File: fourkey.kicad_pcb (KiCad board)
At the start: 2 copper layers, 85.3 x 75.7 mm, 20 parts, among them K1 KEYSW, K2 KEYSW, K3 KEYSW, K4 KEYSW, SW1 SW_PUSH, U1 ProMicro

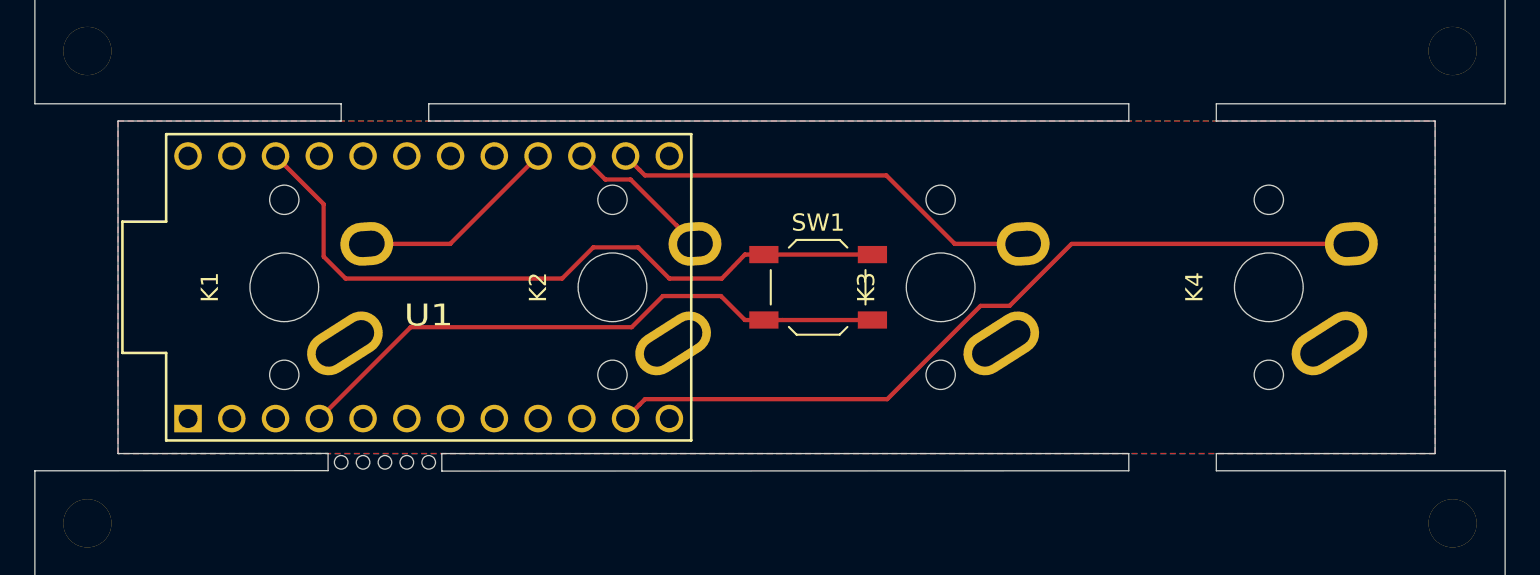
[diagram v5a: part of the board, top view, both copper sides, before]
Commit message: add other mousebites, rounded corners
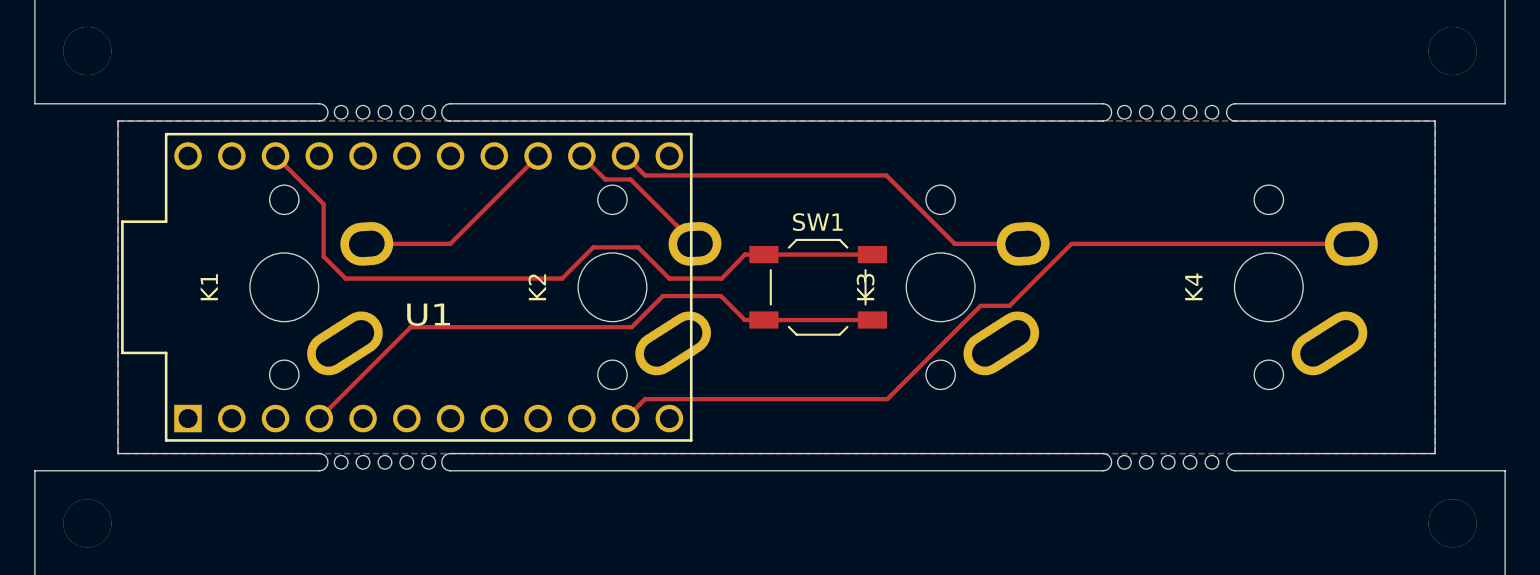
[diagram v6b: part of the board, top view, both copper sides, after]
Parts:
- added REF**: breakaway-mousebites, Keebio-Parts:breakaway-mousebites, F.Cu at (147.3, 76.5)
- added REF**: breakaway-mousebites, Keebio-Parts:breakaway-mousebites, F.Cu at (192.8, 76.5)
- added REF**: breakaway-mousebites, Keebio-Parts:breakaway-mousebites, F.Cu at (192.8, 96.8)
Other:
- outline, holes or cut-outs redrawn
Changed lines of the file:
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@@
   (general
     (thickness 1.6)
-    (drawings 35)
+    (drawings 28)
     (tracks 38)
     (zones 0)
-    (modules 20)
+    (modules 23)
     (nets 27)
   )
@@
     (add_net "Net-(U1-Pad9)")
     (add_net VCC)
+  )
+  (module Keebio-Parts:breakaway-mousebites (layer F.Cu)
+    (at 147.32 76.454)
+    (fp_text reference REF** (at 0 -3.048) (layer Dwgs.User) hide
+      (effects (font (size 1 1) (thickness 0.15)))
+    )
+    (fp_text value breakaway-mousebites (at 0 -4.75) (layer F.Fab) hide
+      (effects (font (size 1 1) (thickness 0.15)))
+    )
+    (fp_line (start -2.794 0) (end 2.794 0) (layer Dwgs.User) (width 0.15))
+    (pad "" np_thru_hole circle (at -2.54 -0.254) (size 0.7874 0.7874) (drill 0.7874) (layers *.Cu *.Mask))
+    (pad "" np_thru_hole circle (at -1.27 -0.254) (size 0.7874 0.7874) (drill 0.7874) (layers *.Cu *.Mask))
+    (pad "" np_thru_hole circle (at 2.54 -0.254) (size 0.7874 0.7874) (drill 0.7874) (layers *.Cu *.Mask))
+    (pad "" np_thru_hole circle (at 1.27 -0.254) (size 0.7874 0.7874) (drill 0.7874) (layers *.Cu *.Mask))
+    (pad "" np_thru_hole circle (at 0 -0.254) (size 0.7874 0.7874) (drill 0.7874) (layers *.Cu *.Mask))
+  )
+  (module Keebio-Parts:breakaway-mousebites (layer F.Cu)
+    (at 192.786 76.454)
+    (fp_text reference REF** (at 0 -3.048) (layer Dwgs.User) hide
+      (effects (font (size 1 1) (thickness 0.15)))
+    )
+    (fp_text value breakaway-mousebites (at 0 -4.75) (layer F.Fab) hide
+      (effects (font (size 1 1) (thickness 0.15)))
+    )
+    (fp_line (start -2.794 0) (end 2.794 0) (layer Dwgs.User) (width 0.15))
+    (pad "" np_thru_hole circle (at -2.54 -0.254) (size 0.7874 0.7874) (drill 0.7874) (layers *.Cu *.Mask))
+    (pad "" np_thru_hole circle (at -1.27 -0.254) (size 0.7874 0.7874) (drill 0.7874) (layers *.Cu *.Mask))
+    (pad "" np_thru_hole circle (at 2.54 -0.254) (size 0.7874 0.7874) (drill 0.7874) (layers *.Cu *.Mask))
+    (pad "" np_thru_hole circle (at 1.27 -0.254) (size 0.7874 0.7874) (drill 0.7874) (layers *.Cu *.Mask))
+    (pad "" np_thru_hole circle (at 0 -0.254) (size 0.7874 0.7874) (drill 0.7874) (layers *.Cu *.Mask))
+  )
+  (module Keebio-Parts:breakaway-mousebites (layer F.Cu)
+    (at 192.786 96.774)
+    (fp_text reference REF** (at 0 -3.048) (layer Dwgs.User) hide
+      (effects (font (size 1 1) (thickness 0.15)))
+    )
+    (fp_text value breakaway-mousebites (at 0 -4.75) (layer F.Fab) hide
+      (effects (font (size 1 1) (thickness 0.15)))
+    )
+    (fp_line (start -2.794 0) (end 2.794 0) (layer Dwgs.User) (width 0.15))
+    (pad "" np_thru_hole circle (at -2.54 -0.254) (size 0.7874 0.7874) (drill 0.7874) (layers *.Cu *.Mask))
+    (pad "" np_thru_hole circle (at -1.27 -0.254) (size 0.7874 0.7874) (drill 0.7874) (layers *.Cu *.Mask))
+    (pad "" np_thru_hole circle (at 2.54 -0.254) (size 0.7874 0.7874) (drill 0.7874) (layers *.Cu *.Mask))
+    (pad "" np_thru_hole circle (at 1.27 -0.254) (size 0.7874 0.7874) (drill 0.7874) (layers *.Cu *.Mask))
+    (pad "" np_thru_hole circle (at 0 -0.254) (size 0.7874 0.7874) (drill 0.7874) (layers *.Cu *.Mask))
   )
   (module keyboard_parts:HOLE_M3 (layer F.Cu)
@@
     )
   )
+  (gr_arc (start 151.122 76.208) (end 151.122 75.708) (angle -180) (layer Edge.Cuts) (width 0.05))
+  (gr_arc (start 143.51 76.208) (end 143.51 75.708) (angle 180) (layer Edge.Cuts) (width 0.05))
+  (gr_arc (start 196.68 76.208) (end 196.68 75.708) (angle -180) (layer Edge.Cuts) (width 0.05))
+  (gr_arc (start 189 76.208) (end 189 75.708) (angle 180) (layer Edge.Cuts) (width 0.05))
+  (gr_arc (start 196.68 96.512) (end 196.68 96.012001) (angle -180) (layer Edge.Cuts) (width 0.05))
+  (gr_arc (start 189 96.512) (end 189 96.012001) (angle 180) (layer Edge.Cuts) (width 0.05))
+  (gr_arc (start 151.122 96.512) (end 151.122 96.012) (angle -180) (layer Edge.Cuts) (width 0.05))
+  (gr_arc (start 143.51 96.512) (end 143.51 96.012) (angle 180) (layer Edge.Cuts) (width 0.05))
   (gr_line (start 212.344 124.19) (end 127 124.19) (layer Edge.Cuts) (width 0.05))
-  (gr_line (start 195.58 96.52) (end 195.58 96.52) (layer Edge.Cuts) (width 0.05))
   (gr_line (start 212.344 97.012) (end 212.344 124.19) (layer Edge.Cuts) (width 0.05))
-  (gr_line (start 190.5 96.012) (end 190.5 97.012) (layer Edge.Cuts) (width 0.05))
-  (gr_line (start 190.5 96.52) (end 190.5 96.52) (layer Edge.Cuts) (width 0.05))
-  (gr_line (start 127 97.012) (end 144.018 97.004) (layer Edge.Cuts) (width 0.05))
+  (gr_line (start 127 97.012) (end 143.51 97.012) (layer Edge.Cuts) (width 0.05))
   (gr_line (start 127 97.012) (end 127 124.19) (layer Edge.Cuts) (width 0.05))
-  (gr_line (start 150.622 96.012) (end 150.622 97.028) (layer Edge.Cuts) (width 0.05))
-  (gr_line (start 195.58 96.012) (end 195.58 97.012) (layer Edge.Cuts) (width 0.05))
-  (gr_line (start 195.58 97.012) (end 212.344 97.012) (layer Edge.Cuts) (width 0.05))
-  (gr_line (start 144.018 96.004) (end 144.018 97.004) (layer Edge.Cuts) (width 0.05))
-  (gr_line (start 150.622 97.028) (end 190.5 97.012) (layer Edge.Cuts) (width 0.05))
-  (gr_line (start 195.58 96.52) (end 195.58 96.52) (layer Edge.Cuts) (width 0.05))
-  (gr_line (start 195.58 96.012) (end 208.28 96.012) (layer Edge.Cuts) (width 0.05))
-  (gr_line (start 150.622 96.012) (end 190.5 96.012) (layer Edge.Cuts) (width 0.05))
-  (gr_line (start 195.58 75.708) (end 195.58 76.708) (layer Edge.Cuts) (width 0.05))
-  (gr_line (start 190.5 75.708) (end 190.5 76.708) (layer Edge.Cuts) (width 0.05))
-  (gr_line (start 190.5 76.708) (end 149.86 76.708) (layer Edge.Cuts) (width 0.05))
-  (gr_line (start 190.5 75.692) (end 190.5 75.692) (layer Edge.Cuts) (width 0.05))
-  (gr_line (start 195.58 75.692) (end 195.58 75.692) (layer Edge.Cuts) (width 0.05))
-  (gr_line (start 195.58 75.708) (end 212.344 75.708) (layer Edge.Cuts) (width 0.05))
-  (gr_line (start 144.78 76.708) (end 131.826 76.708) (layer Edge.Cuts) (width 0.05))
-  (gr_line (start 149.86 75.692) (end 149.86 75.692) (layer Edge.Cuts) (width 0.05))
-  (gr_line (start 149.86 75.708) (end 190.5 75.708) (layer Edge.Cuts) (width 0.05))
-  (gr_line (start 149.86 75.692) (end 149.86 75.692) (layer Edge.Cuts) (width 0.05))
-  (gr_line (start 149.86 75.708) (end 149.86 76.708) (layer Edge.Cuts) (width 0.05))
-  (gr_line (start 144.78 76.708) (end 144.78 75.708) (layer Edge.Cuts) (width 0.05))
+  (gr_line (start 196.68 97.012) (end 212.344 97.012) (layer Edge.Cuts) (width 0.05))
+  (gr_line (start 151.122 97.012) (end 189 97.012) (layer Edge.Cuts) (width 0.05))
+  (gr_line (start 196.68 96.012) (end 208.28 96.012) (layer Edge.Cuts) (width 0.05))
+  (gr_line (start 151.122 96.012) (end 189 96.012) (layer Edge.Cuts) (width 0.05))
+  (gr_line (start 189 76.708) (end 151.122 76.708) (layer Edge.Cuts) (width 0.05))
+  (gr_line (start 196.68 75.708) (end 212.344 75.708) (layer Edge.Cuts) (width 0.05))
+  (gr_line (start 143.51 76.708) (end 131.826 76.708) (layer Edge.Cuts) (width 0.05))
+  (gr_line (start 151.122 75.708) (end 189 75.708) (layer Edge.Cuts) (width 0.05))
   (gr_line (start 212.344 48.53) (end 127 48.53) (layer Edge.Cuts) (width 0.05))
   (gr_line (start 127 48.53) (end 127 75.708) (layer Edge.Cuts) (width 0.05))
-  (gr_line (start 127 75.708) (end 144.78 75.708) (layer Edge.Cuts) (width 0.05))
+  (gr_line (start 127 75.708) (end 143.51 75.708) (layer Edge.Cuts) (width 0.05))
   (gr_line (start 212.344 75.708) (end 212.344 48.53) (layer Edge.Cuts) (width 0.05))
   (gr_line (start 208.28 96.012) (end 208.28 76.708) (layer Edge.Cuts) (width 0.05))
-  (gr_line (start 131.826 96.012) (end 144.018 96.004) (layer Edge.Cuts) (width 0.05))
+  (gr_line (start 131.826 96.012) (end 143.51 96.012) (layer Edge.Cuts) (width 0.05))
   (gr_line (start 131.826 76.708) (end 131.826 96.012) (layer Edge.Cuts) (width 0.05))
-  (gr_line (start 208.28 76.708) (end 195.58 76.708) (layer Edge.Cuts) (width 0.05))
+  (gr_line (start 208.28 76.708) (end 196.68 76.708) (layer Edge.Cuts) (width 0.05))
   (segment (start 151.11 83.84) (end 156.21 78.74) (width 0.25) (layer F.Cu) (net 2))
   (segment (start 146.268 83.84) (end 151.11 83.84) (width 0.25) (layer F.Cu) (net 2))

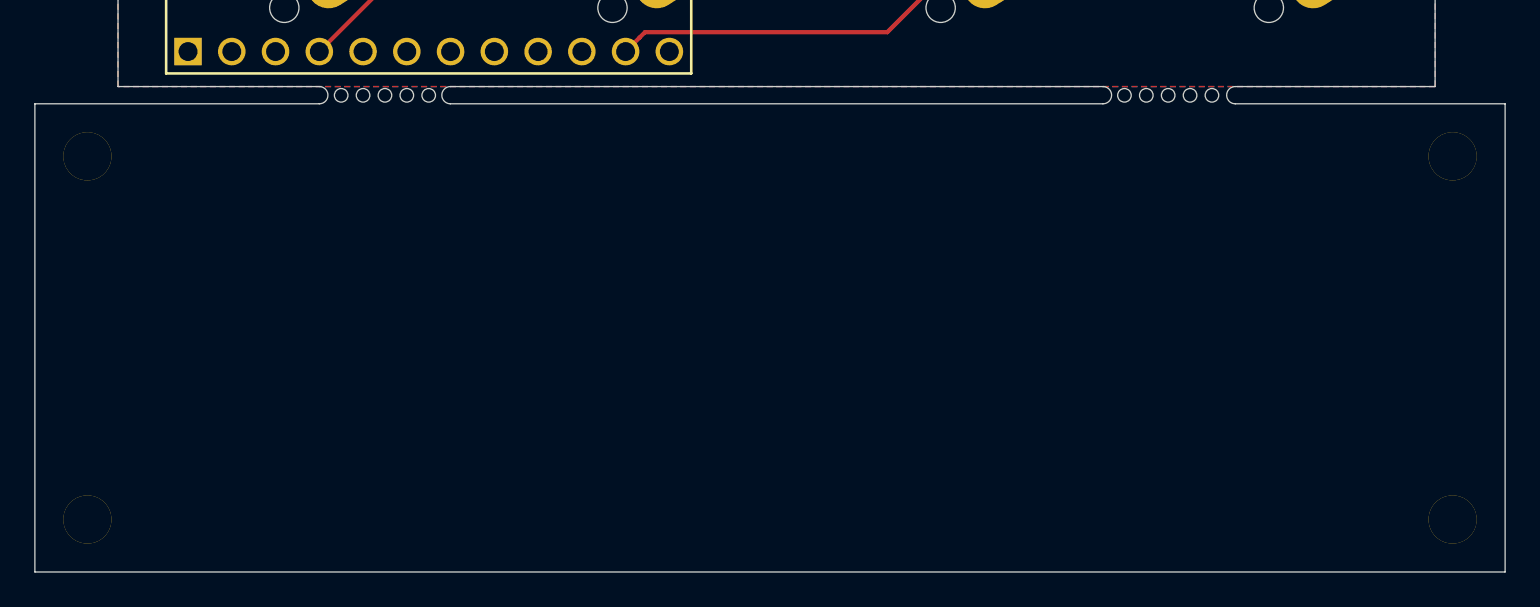
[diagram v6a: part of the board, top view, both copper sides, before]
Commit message: more rounded corners
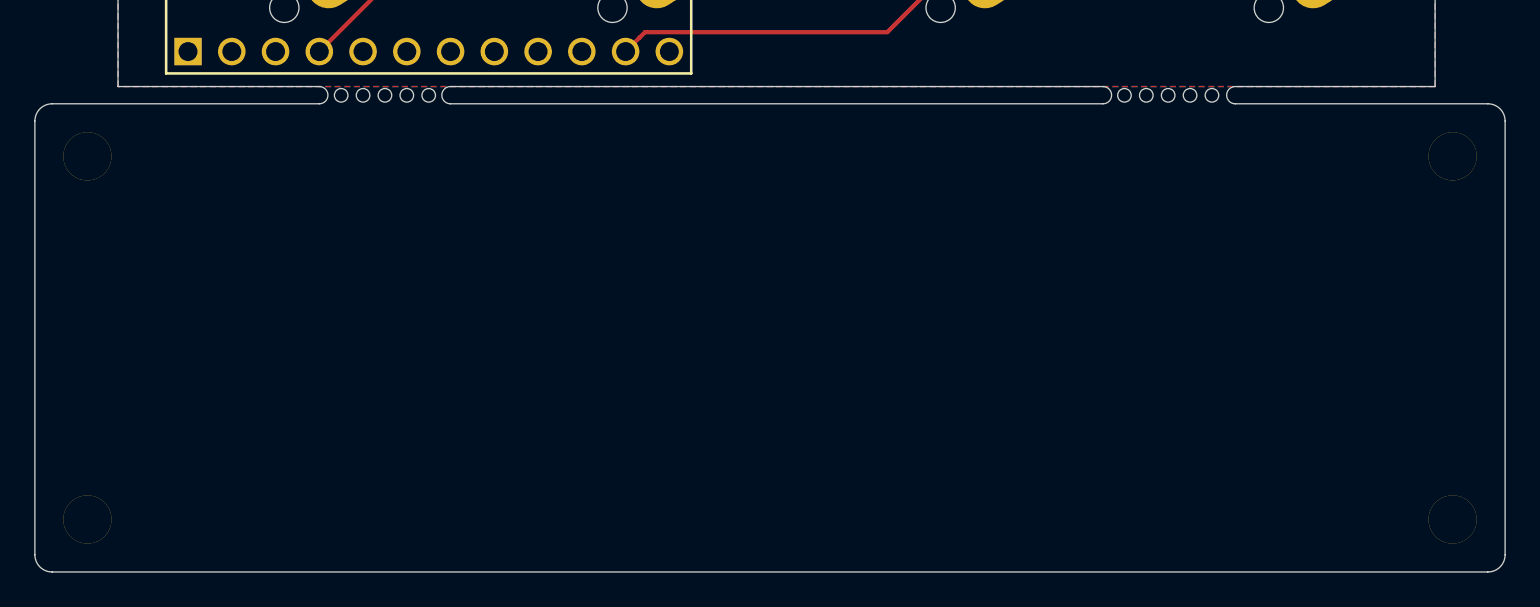
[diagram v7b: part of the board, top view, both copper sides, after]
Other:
- outline, holes or cut-outs redrawn
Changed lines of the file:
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@@
   (general
     (thickness 1.6)
-    (drawings 28)
+    (drawings 32)
     (tracks 38)
     (zones 0)
@@
     )
   )
+  (gr_arc (start 211.344 98.012) (end 212.344 98.012) (angle -90) (layer Edge.Cuts) (width 0.05))
+  (gr_arc (start 211.344 123.19) (end 212.344 123.19) (angle 90) (layer Edge.Cuts) (width 0.05))
+  (gr_arc (start 128 123.19) (end 127 123.19) (angle -90) (layer Edge.Cuts) (width 0.05))
+  (gr_arc (start 128 98.012) (end 128 97.012) (angle -90) (layer Edge.Cuts) (width 0.05))
   (gr_arc (start 151.122 76.208) (end 151.122 75.708) (angle -180) (layer Edge.Cuts) (width 0.05))
   (gr_arc (start 143.51 76.208) (end 143.51 75.708) (angle 180) (layer Edge.Cuts) (width 0.05))
@@
   (gr_arc (start 151.122 96.512) (end 151.122 96.012) (angle -180) (layer Edge.Cuts) (width 0.05))
   (gr_arc (start 143.51 96.512) (end 143.51 96.012) (angle 180) (layer Edge.Cuts) (width 0.05))
-  (gr_line (start 212.344 124.19) (end 127 124.19) (layer Edge.Cuts) (width 0.05))
-  (gr_line (start 212.344 97.012) (end 212.344 124.19) (layer Edge.Cuts) (width 0.05))
-  (gr_line (start 127 97.012) (end 143.51 97.012) (layer Edge.Cuts) (width 0.05))
-  (gr_line (start 127 97.012) (end 127 124.19) (layer Edge.Cuts) (width 0.05))
-  (gr_line (start 196.68 97.012) (end 212.344 97.012) (layer Edge.Cuts) (width 0.05))
+  (gr_line (start 211.344 124.19) (end 128 124.19) (layer Edge.Cuts) (width 0.05))
+  (gr_line (start 212.344 98.012) (end 212.344 123.19) (layer Edge.Cuts) (width 0.05))
+  (gr_line (start 128 97.012) (end 143.51 97.012) (layer Edge.Cuts) (width 0.05))
+  (gr_line (start 127 98.012) (end 127 123.19) (layer Edge.Cuts) (width 0.05))
+  (gr_line (start 196.68 97.012) (end 211.344 97.012) (layer Edge.Cuts) (width 0.05))
   (gr_line (start 151.122 97.012) (end 189 97.012) (layer Edge.Cuts) (width 0.05))
   (gr_line (start 196.68 96.012) (end 208.28 96.012) (layer Edge.Cuts) (width 0.05))
